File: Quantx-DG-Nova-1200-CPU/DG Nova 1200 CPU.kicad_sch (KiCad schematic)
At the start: 243 parts, among them Q1 MPS3640, U1 74LS122, U10 74LS20, U100 045, U101 74LS04, U102 74LS179, U103 74LS179, U104 8271, U105 74LS179, U106 74LS179, U107 74LS179, U108 74LS179, U109 74LS00, U11 74LS03, U110 74LS20, U111 74LS10, U112 74LS51, U113 74LS114, U114 74LS51, U115 74LS179, U116 74LS157, U117 74LS181, U118 74LS00, U119 74LS170, U12 74LS00, U120 8264, U121 74LS157, U122 74LS179, U123 8225, U124 8225, U125 8264, U13 045, U14 74LS20, U15 74LS20, U16 74LS04, U17 74LS179, U18 74LS20, U19 74LS00, U2 74LS74, U20 74LS74, U21 74LS00, U22 74LS04, U23 74LS179, U24 74LS51, U25 74LS139, U26 74LS04, U27 74LS04, U28 74LS179, U29 74LS179, U3 74LS00, U30 82S23, U31 82S23, U32 74LS179, U33 74LS179, U34 045, U35 74LS10, U36 74LS00, U37 74LS179, U38 74LS179, U39 74LS179, U4 045, U40 74LS179, U41 045, U42 74LS179, U43 74H54, U44 74LS51, U45 74LS51, U46 74H54, U47 74H54, U48 045, U49 74LS03, U5 74LS04, U50 74LS10, U51 74LS139, U52 74LS139, U53 045, U54 74LS179, U55 74LS51, U56 74LS20, U57 74LS00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

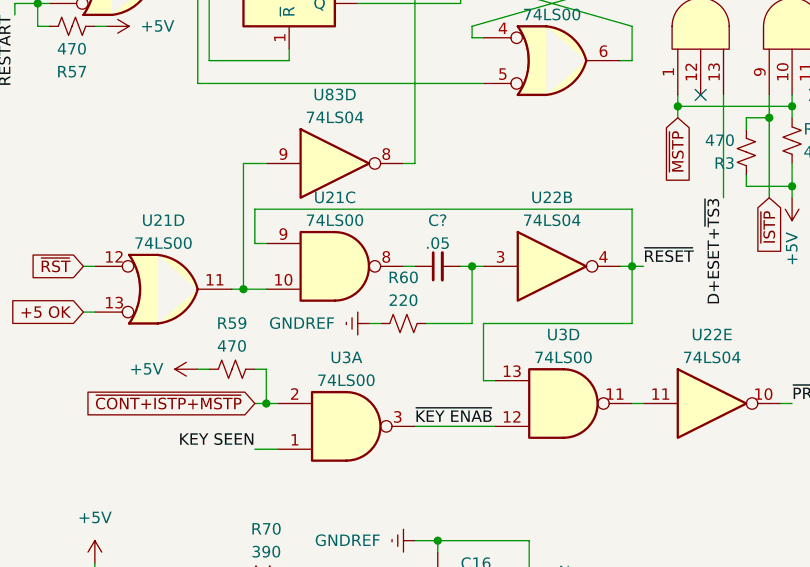
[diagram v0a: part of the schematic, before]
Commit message: Update DG Nova 1200 CPU.kicad_sch
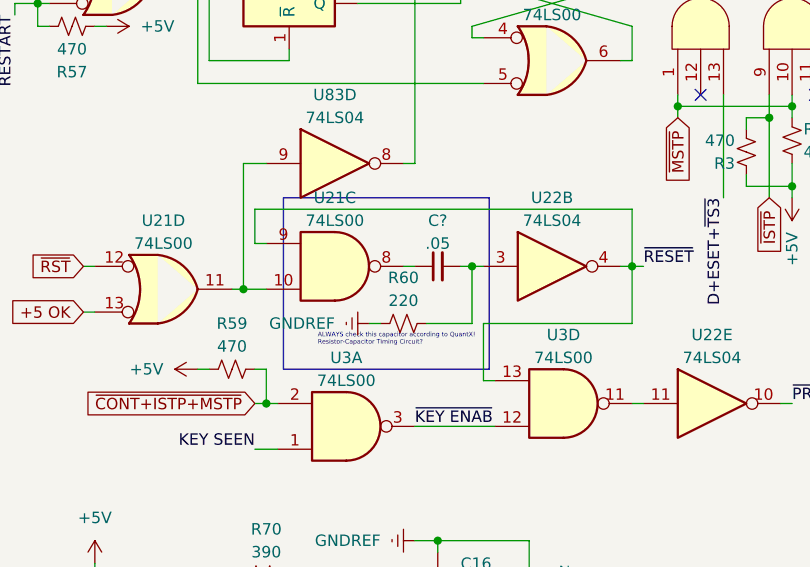
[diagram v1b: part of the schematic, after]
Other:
- note added: "ALWAYS check this capacitor according to QuantX! Resistor-Capacitor Timing Circuit?"
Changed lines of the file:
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@@
     (fill (type none))
   )
+  (rectangle (start 45.085 177.8) (end 67.945 196.85)
+    (stroke (width 0) (type default) (color 255 0 9 1))
+    (fill (type none))
+  )
+  (rectangle (start 67.945 196.85) (end 67.945 196.85)
+    (stroke (width 0) (type default))
+    (fill (type none))
+  )
   (image (at 676.275 267.97) (scale 0.364394)
     (data
@@
     (effects (font (size 1.27 1.27)) (justify left bottom))
   )
+  (text "ALWAYS check this capacitor according to QuantX!\nResistor-Capacitor Timing Circuit?"
+    (at 48.895 194.31 0)
+    (effects (font (size 0.5 0.5) (color 255 7 0 1)) (justify left bottom))
+  )
   (text "This pullup is only needed if\nusing a 74122 instead of a\nFairchild 9601 and is not\npresent on an actual 1200 CPU"
     (at 586.74 416.56 0)
@@
       (effects (font (size 1.27 1.27)) hide)
     )
-    (pin "8")
     (pin "1")
-    (pin "15")
     (pin "10")
-    (pin "4")
-    (pin "14")
+    (pin "11")
+    (pin "12")
     (pin "13")
+    (pin "14")
+    (pin "15")
     (pin "2")
-    (pin "12")
-    (pin "11")
-    (pin "16")
-    (pin "7")
     (pin "3")
-    (pin "6")
+    (pin "4")
     (pin "5")
+    (pin "6")
+    (pin "7")
     (pin "9")
+    (pin "16")
+    (pin "8")
     (instances
       (project "DG Nova 1200 CPU"
@@
       (effects (font (size 1.27 1.27)) hide)
     )
-    (pin "8")
     (pin "1")
-    (pin "15")
     (pin "10")
-    (pin "4")
-    (pin "14")
+    (pin "11")
+    (pin "12")
     (pin "13")
+    (pin "14")
+    (pin "15")
     (pin "2")
-    (pin "12")
-    (pin "11")
-    (pin "16")
-    (pin "7")
     (pin "3")
-    (pin "6")
+    (pin "4")
     (pin "5")
+    (pin "6")
+    (pin "7")
     (pin "9")
+    (pin "16")
+    (pin "8")
     (instances
       (project "DG Nova 1200 CPU"

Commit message: u
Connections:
- net BodgeU82p1: now reaches U2.9 (Q)
- net BodgeU82p1: now also U82.1
- net BodgeU82p2: now reaches U82.2
- net BodgeU82p3: now reaches U82.3
- no-connect marks 129 -> 128
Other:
- moved on the sheet: U82A
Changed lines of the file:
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@@
   (no_connect (at 807.72 491.49))
   (no_connect (at 807.72 488.95))
-  (no_connect (at 647.7 449.58))
   (no_connect (at 181.61 518.16))
   (no_connect (at 369.57 518.16))
@@
     (stroke (width 0) (type default))
   )
+  (wire (pts (xy 647.7 449.58) (xy 659.13 449.58))
+    (stroke (width 0) (type default))
+  )
   (wire (pts (xy 66.04 153.67) (xy 66.04 152.4))
     (stroke (width 0) (type default))
@@
     (effects (font (size 1.27 1.27)) (justify right bottom))
   )
+  (label "MBO13" (at 520.7 210.82 180) (fields_autoplaced)
+    (effects (font (size 1.27 1.27)) (justify right bottom))
+  )
   (label "S2" (at 279.4 309.88 0) (fields_autoplaced)
     (effects (font (size 1.27 1.27)) (justify left bottom))
@@
     (effects (font (size 1.27 1.27)) (justify right bottom))
   )
+  (label "MBO15" (at 549.275 295.91 180) (fields_autoplaced)
+    (effects (font (size 1.27 1.27)) (justify right bottom))
+  )
   (label "ACB11" (at 778.51 361.95 0) (fields_autoplaced)
     (effects (font (size 1.27 1.27)) (justify left bottom))
@@
     (effects (font (size 1.27 1.27)) (justify right bottom))
   )
+  (label "MBO12" (at 548.64 280.67 180) (fields_autoplaced)
+    (effects (font (size 1.27 1.27)) (justify right bottom))
+  )
   (label "DCH" (at 363.22 140.97 180) (fields_autoplaced)
     (effects (font (size 1.27 1.27)) (justify right bottom))
@@
     (effects (font (size 1.27 1.27)) (justify left bottom))
   )
+  (label "MBO13" (at 549.275 288.29 180) (fields_autoplaced)
+    (effects (font (size 1.27 1.27)) (justify right bottom))
+  )
   (label "FETCH" (at 675.64 71.12 180) (fields_autoplaced)
     (effects (font (size 1.27 1.27)) (justify right bottom))
@@
     (effects (font (size 1.27 1.27)) (justify right bottom))
   )
+  (label "MBO14" (at 549.275 303.53 180) (fields_autoplaced)
+    (effects (font (size 1.27 1.27)) (justify right bottom))
+  )
   (label "ADDER3" (at 758.19 361.95 180) (fields_autoplaced)
     (effects (font (size 1.27 1.27)) (justify right bottom))
@@
     )
   )
-  (global_label "MBO12" (shape input) (at 548.64 280.67 180) (fields_autoplaced)
-    (effects (font (size 1.27 1.27)) (justify right))
-    (property "Intersheetrefs" "${INTERSHEET_REFS}" (at 539.7559 280.5906 0)
-      (effects (font (size 1.27 1.27)) (justify right) hide)
-    )
-  )
   (global_label "~{RST}" (shape input) (at 22.86 185.42 180) (fields_autoplaced)
     (effects (font (size 1.27 1.27)) (justify right))
@@
     )
   )
+  (global_label "BodgeU82p1" (shape input) (at 808.99 433.705 180) (fields_autoplaced)
+    (effects (font (size 1.27 1.27)) (justify right))
+    (property "Intersheetrefs" "${INTERSHEET_REFS}" (at 794.1706 433.705 0)
+      (effects (font (size 1.27 1.27)) (justify right) hide)
+    )
+  )
   (global_label "~{INTR}" (shape input) (at 212.09 505.46 90) (fields_autoplaced)
     (effects (font (size 1.27 1.27)) (justify left))
@@
     )
   )
-  (global_label "MBO13" (shape input) (at 548.64 288.29 180) (fields_autoplaced)
-    (effects (font (size 1.27 1.27)) (justify right))
-    (property "Intersheetrefs" "${INTERSHEET_REFS}" (at 539.7559 288.2106 0)
-      (effects (font (size 1.27 1.27)) (justify right) hide)
-    )
-  )
   (global_label "~{DATA11}" (shape input) (at 176.53 518.16 270) (fields_autoplaced)
     (effects (font (size 1.27 1.27)) (justify right))
@@
     )
   )
-  (global_label "MBO14" (shape input) (at 548.64 303.53 180) (fields_autoplaced)
-    (effects (font (size 1.27 1.27)) (justify right))
-    (property "Intersheetrefs" "${INTERSHEET_REFS}" (at 539.7559 303.4506 0)
-      (effects (font (size 1.27 1.27)) (justify right) hide)
-    )
-  )
   (global_label "~{DATA4}" (shape input) (at 518.16 499.11 90) (fields_autoplaced)
     (effects (font (size 1.27 1.27)) (justify left))
@@
     )
   )
+  (global_label "BodgeU82p3" (shape input) (at 824.23 436.245 0) (fields_autoplaced)
+    (effects (font (size 1.27 1.27)) (justify left))
+    (property "Intersheetrefs" "${INTERSHEET_REFS}" (at 839.0494 436.245 0)
+      (effects (font (size 1.27 1.27)) (justify left) hide)
+    )
+  )
   (global_label "~{MEM7}" (shape input) (at 219.71 518.16 270) (fields_autoplaced)
     (effects (font (size 1.27 1.27)) (justify right))
@@
     )
   )
-  (global_label "MBO15" (shape input) (at 548.64 295.91 180) (fields_autoplaced)
-    (effects (font (size 1.27 1.27)) (justify right))
-    (property "Intersheetrefs" "${INTERSHEET_REFS}" (at 539.7559 295.8306 0)
-      (effects (font (size 1.27 1.27)) (justify right) hide)
-    )
-  )
   (global_label "~{MEM8}" (shape input) (at 311.15 505.46 90) (fields_autoplaced)
     (effects (font (size 1.27 1.27)) (justify left))
@@
     )
   )
+  (global_label "BodgeU82p2" (shape input) (at 808.99 438.785 180) (fields_autoplaced)
+    (effects (font (size 1.27 1.27)) (justify right))
+    (property "Intersheetrefs" "${INTERSHEET_REFS}" (at 794.1706 438.785 0)
+      (effects (font (size 1.27 1.27)) (justify right) hide)
+    )
+  )
   (global_label "~{MBO11}" (shape input) (at 242.57 505.46 90) (fields_autoplaced)
     (effects (font (size 1.27 1.27)) (justify left))
@@
     )
   )
+  (global_label "BodgeU82p1" (shape input) (at 659.13 449.58 0) (fields_autoplaced)
+    (effects (font (size 1.27 1.27)) (justify left))
+    (property "Intersheetrefs" "${INTERSHEET_REFS}" (at 673.9494 449.58 0)
+      (effects (font (size 1.27 1.27)) (justify left) hide)
+    )
+  )
   (global_label "~{SHIFT0}" (shape output) (at 523.24 405.13 0) (fields_autoplaced)
     (effects (font (size 1.27 1.27)) (justify left))
@@
     )
   )
-  (symbol (lib_id "74xx:74LS00") (at 815.34 473.71 0) (unit 1)
+  (symbol (lib_id "74xx:74LS00") (at 816.61 436.245 0) (unit 1)
     (in_bom yes) (on_board yes) (dnp no) (fields_autoplaced)
-    (property "Reference" "U82" (at 815.34 464.82 0)
+    (property "Reference" "U82" (at 816.61 427.355 0)
       (effects (font (size 1.27 1.27)))
     )
-    (property "Value" "74LS00" (at 815.34 467.36 0)
+    (property "Value" "74LS00" (at 816.61 429.895 0)
       (effects (font (size 1.27 1.27)))
     )
-    (property "Footprint" "" (at 815.34 473.71 0)
+    (property "Footprint" "" (at 816.61 436.245 0)
       (effects (font (size 1.27 1.27)) hide)
     )
-    (property "Datasheet" "http://www.ti.com/lit/gpn/sn74ls00" (at 815.34 473.71 0)
+    (property "Datasheet" "http://www.ti.com/lit/gpn/sn74ls00" (at 816.61 436.245 0)
       (effects (font (size 1.27 1.27)) hide)
     )
